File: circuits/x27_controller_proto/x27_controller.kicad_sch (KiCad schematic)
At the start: 15 parts, among them J1 INPUT, J2 5V, M1 x27_Stepper, U1 74HC595

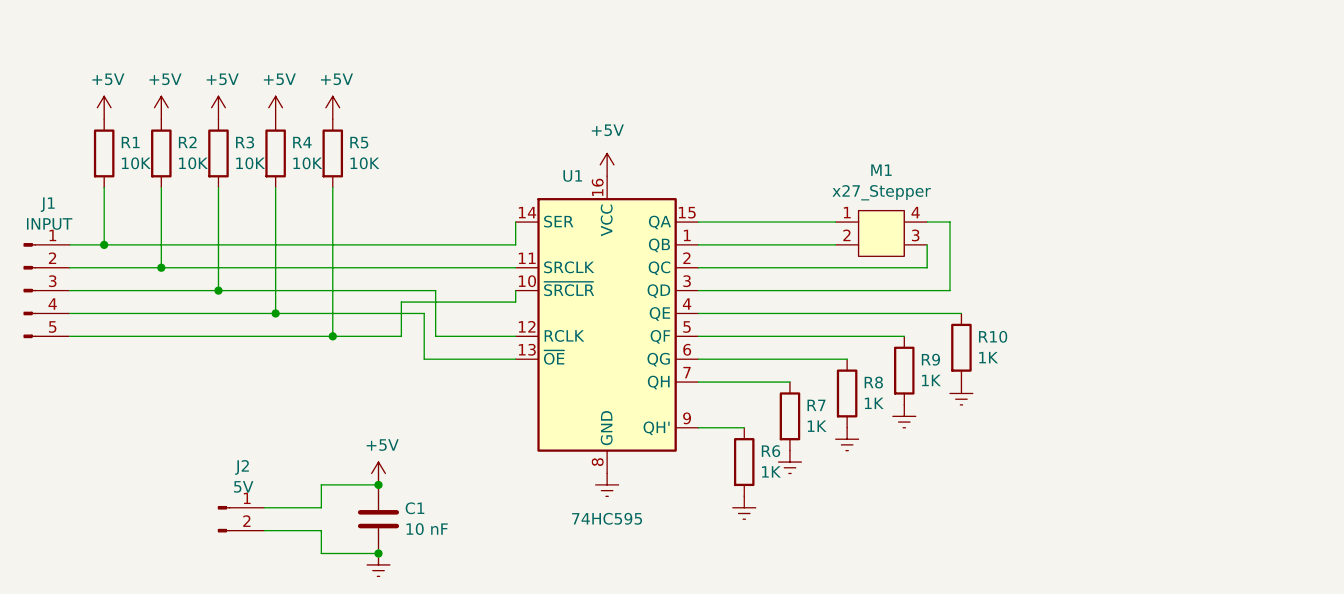
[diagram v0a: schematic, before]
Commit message: Code works and is tested on waveforms.
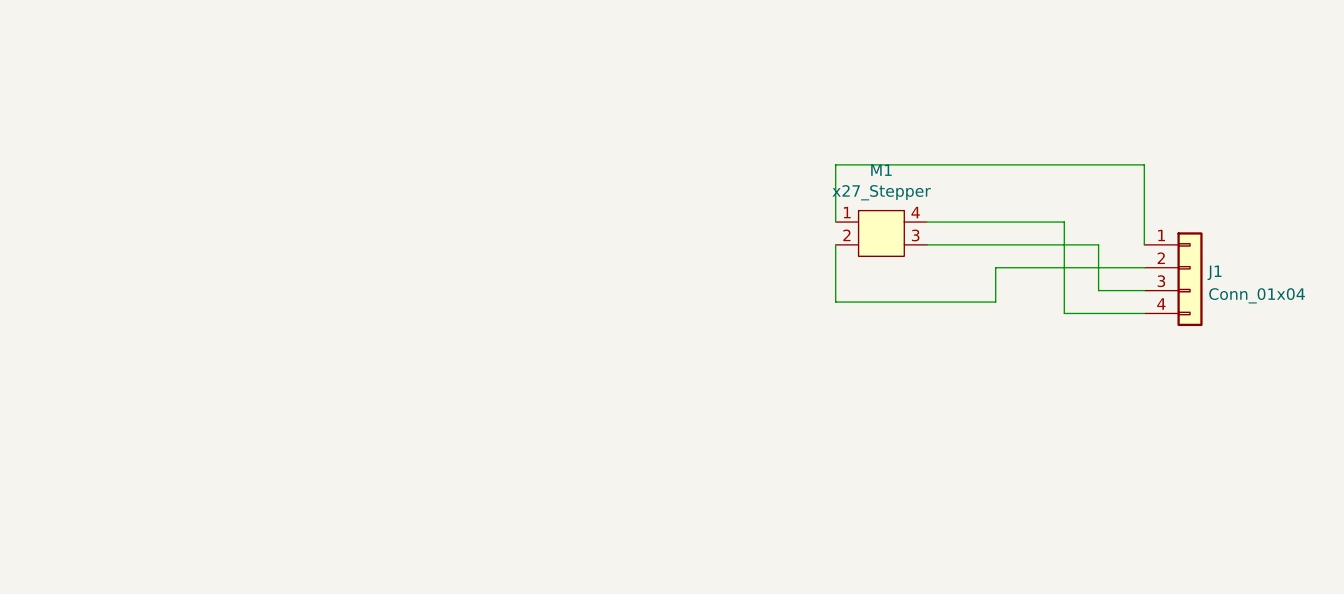
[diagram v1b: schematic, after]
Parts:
- removed C1: 10 nF, Capacitor_SMD:C_0805_2012Metric_Pad1.18x1.45mm_HandSolder, symbol Device:C
- removed J1: INPUT, Connector_PinHeader_2.54mm:PinHeader_1x05_P2.54mm_Vertical, symbol Connector:Conn_01x05_Male
- removed J2: 5V, Connector_PinHeader_2.54mm:PinHeader_1x02_P2.54mm_Vertical, symbol Connector:Conn_01x02_Male
- removed R1, R2, R3, R4, R5: 10K, Resistor_SMD:R_0805_2012Metric_Pad1.20x1.40mm_HandSolder, symbol Device:R
- removed R10, R6, R7, R8, R9: 1K, Resistor_SMD:R_0805_2012Metric_Pad1.20x1.40mm_HandSolder, symbol Device:R
- removed U1: 74HC595, Package_SO:SO-16_3.9x9.9mm_P1.27mm, symbol 74xx:74HC595
- added J1: Conn_01x04, Connector_PinHeader_2.54mm:PinHeader_1x04_P2.54mm_Vertical, symbol Connector_Generic:Conn_01x04
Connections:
- net at M1.1: now also J1.1 (Pin_1)
- net at M1.2: now also J1.2 (Pin_2)
- net at M1.3: now also J1.3 (Pin_3)
- net at M1.4: now also J1.4 (Pin_4)

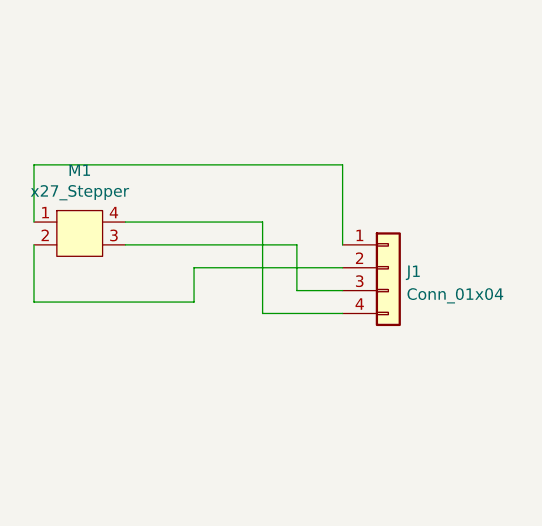
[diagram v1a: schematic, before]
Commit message: Added more pullups
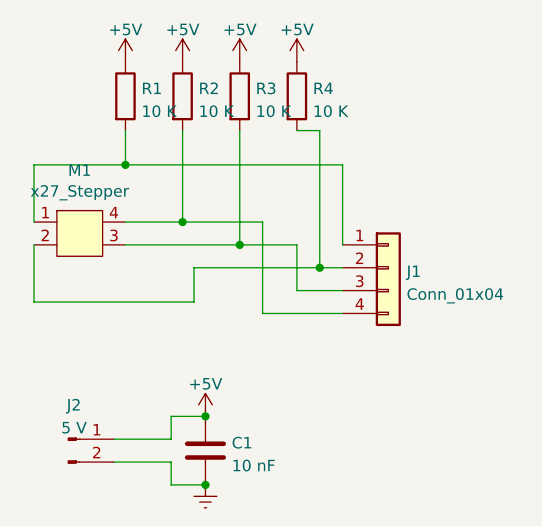
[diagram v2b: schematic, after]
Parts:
- added C1: 10 nF, Capacitor_SMD:C_0805_2012Metric_Pad1.18x1.45mm_HandSolder, symbol Device:C
- added J2: 5 V, Connector_PinHeader_2.54mm:PinHeader_1x02_P2.54mm_Vertical, symbol Connector:Conn_01x02_Male
- added R1, R2, R3, R4: 10 K, Resistor_SMD:R_0805_2012Metric_Pad1.20x1.40mm_HandSolder, symbol Device:R
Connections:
- net at J1.1 (Pin_1), M1.1: now also R1.2
- net at J1.2 (Pin_2), M1.2: now also R4.2
- net at J1.3 (Pin_3), M1.3: now also R3.2
- net at J1.4 (Pin_4), M1.4: now also R2.2
- new net +5V: C1.1, J2.1 (Pin_1), R1.1, R2.1, R3.1, R4.1
- new net Earth: C1.2, J2.2 (Pin_2)
